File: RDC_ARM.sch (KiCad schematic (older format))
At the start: 38 parts, among them J1 RESOLVER ARM, Q1 BC807, Q2 BC807, U1 AD8397ARZ, X1 8.192MHz

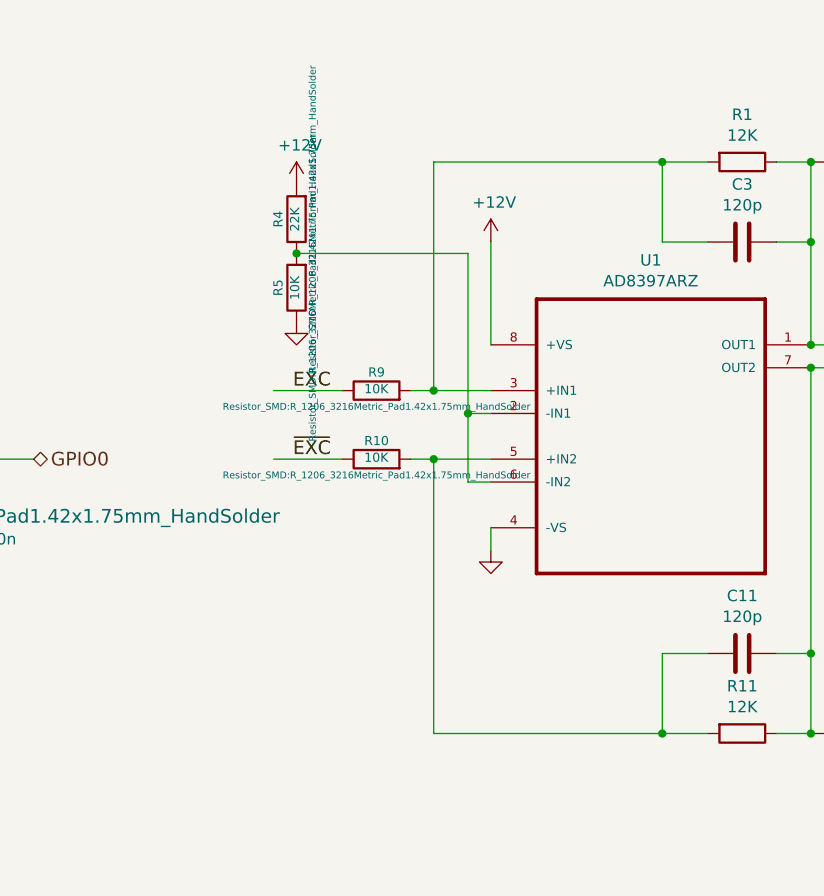
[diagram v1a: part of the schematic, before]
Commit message: Se arregló conexion erronea en los amplificadores operacionales
se agregó conexión 1-wire en GPIO8
se agregó botón y led que comparten GPIO7, la idea es leer el estado del
botón y al liberarlo cambiar el GPIO a output y encender el led indicando
alguna acción
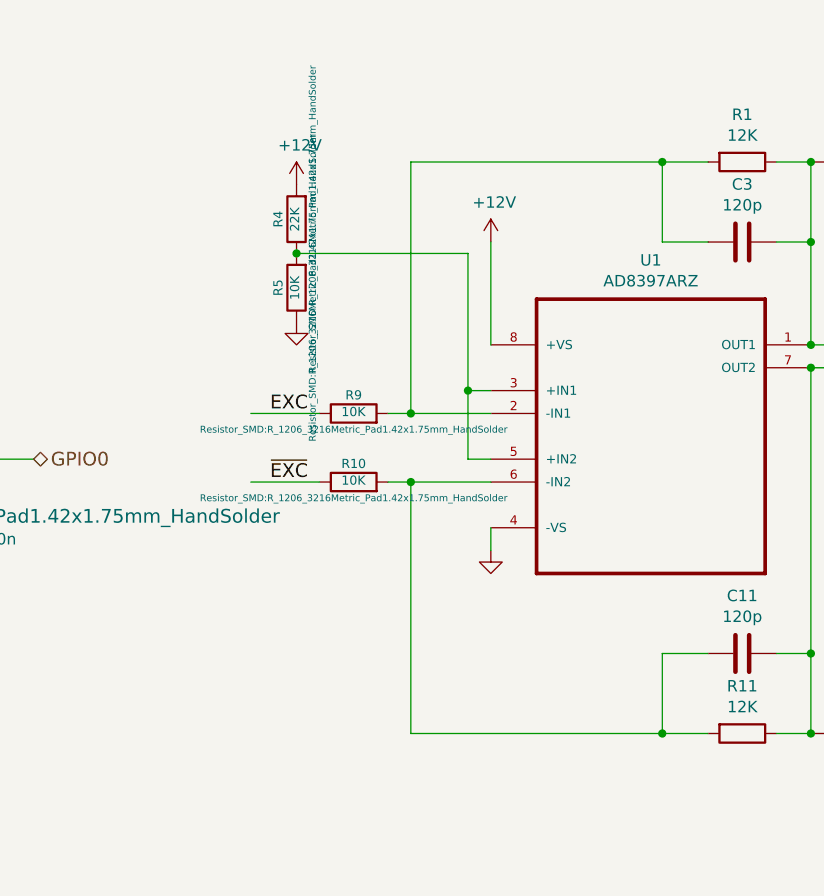
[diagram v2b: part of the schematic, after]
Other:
- moved on the sheet: R10, R9
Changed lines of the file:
@@
 Wire Wire Line
 	8550 4550 8550 4650
-Text Label 7850 4250 2    60   ~ 0
+Text Label 7750 4350 2    60   ~ 0
 ~EXC
-Wire Wire Line
-	8450 4350 8550 4350
 Wire Wire Line
 	7700 3350 8450 3350
@@
 	9950 5450 9800 5450
 Wire Wire Line
-	8300 4250 8550 4250
-Wire Wire Line
 	4750 2050 5100 2050
 Connection ~ 4750 2050
@@
 L Device:R R?
 U 1 1 5F08F1F2
-P 8050 4250
+P 7950 4350
 AR Path="/5F08F1F2" Ref="R?"  Part="1"
 AR Path="/5EF45E27/5F08F1F2" Ref="R10"  Part="1"
 AR Path="/5F077C82/5F08F1F2" Ref="R?"  Part="1"
-F 0 "R10" V 8130 4250 40  0000 C CNN
-F 1 "10K" V 8057 4251 40  0000 C CNN
-F 2 "Resistor_SMD:R_1206_3216Metric_Pad1.42x1.75mm_HandSolder" V 7980 4250 30  0000 C CNN
-F 3 "~" H 8050 4250 30  0000 C CNN
-	1    8050 4250
+F 0 "R10" V 8030 4350 40  0000 C CNN
+F 1 "10K" V 7957 4351 40  0000 C CNN
+F 2 "Resistor_SMD:R_1206_3216Metric_Pad1.42x1.75mm_HandSolder" V 7880 4350 30  0000 C CNN
+F 3 "~" H 7950 4350 30  0000 C CNN
+	1    7950 4350
 	0    -1   -1   0
 $EndComp
@@
 L Device:R R?
 U 1 1 5F08F1F3
-P 8050 3950
+P 7950 4050
 AR Path="/5F08F1F3" Ref="R?"  Part="1"
 AR Path="/5EF45E27/5F08F1F3" Ref="R9"  Part="1"
 AR Path="/5F077C82/5F08F1F3" Ref="R?"  Part="1"
-F 0 "R9" V 8130 3950 40  0000 C CNN
-F 1 "10K" V 8057 3951 40  0000 C CNN
-F 2 "Resistor_SMD:R_1206_3216Metric_Pad1.42x1.75mm_HandSolder" V 7980 3950 30  0000 C CNN
-F 3 "~" H 8050 3950 30  0000 C CNN
-	1    8050 3950
+F 0 "R9" V 8030 4050 40  0000 C CNN
+F 1 "10K" V 7957 4051 40  0000 C CNN
+F 2 "Resistor_SMD:R_1206_3216Metric_Pad1.42x1.75mm_HandSolder" V 7880 4050 30  0000 C CNN
+F 3 "~" H 7950 4050 30  0000 C CNN
+	1    7950 4050
 	0    -1   -1   0
 $EndComp
@@
 	8550 3300 8550 3750
 Wire Wire Line
-	8200 3950 8300 3950
-Connection ~ 8300 3950
-Wire Wire Line
-	8200 4250 8300 4250
-Connection ~ 8300 4250
-Wire Wire Line
-	7600 3950 7900 3950
-Wire Wire Line
-	7900 4250 7600 4250
+	8100 4050 8200 4050
+Connection ~ 8200 4050
+Wire Wire Line
+	8100 4350 8200 4350
+Connection ~ 8200 4350
+Wire Wire Line
+	7500 4050 7800 4050
+Wire Wire Line
+	7800 4350 7500 4350
 Text Label 10600 4350 2    60   ~ 0
 COS
@@
 Wire Wire Line
 	9300 2950 9500 2950
-Wire Wire Line
-	8300 2950 9300 2950
 $Comp
 L power:GND #PWR?
@@
 Wire Wire Line
 	9300 5450 9500 5450
-Wire Wire Line
-	8300 5450 9300 5450
 Connection ~ 9300 5450
 Wire Wire Line
-	8300 4250 8300 5450
+	8200 4350 8200 5450
 Wire Wire Line
 	9950 3850 9950 5100
@@
 Text Notes 4450 2700 0    60   ~ 0
 A0/A1\n 0  0 Normal mode—position output\n 0  1 Normal mode—velocity output\n 1  0 Reserved\n 1  1 Configuration mode
-Connection ~ 8450 4050
-Wire Wire Line
-	8450 4050 8450 4350
-Wire Wire Line
-	8450 4050 8550 4050
-Wire Wire Line
-	8300 2950 8300 3950
-Wire Wire Line
-	8300 3950 8550 3950
-Wire Wire Line
-	8450 3350 8450 4050
-Text Label 7850 3950 2    60   ~ 0
+Text Label 7750 4050 2    60   ~ 0
 EXC
 Wire Wire Line
@@
 	1    0    0    -1
 $EndComp
+Wire Wire Line
+	8200 4350 8550 4350
+Wire Wire Line
+	8200 2950 9300 2950
+Wire Wire Line
+	8200 2950 8200 4050
+Wire Wire Line
+	8200 4050 8550 4050
+Wire Wire Line
+	8550 4250 8450 4250
+Wire Wire Line
+	8450 4250 8450 3950
+Wire Wire Line
+	8550 3950 8450 3950
+Connection ~ 8450 3950
+Wire Wire Line
+	8450 3950 8450 3350
+Wire Wire Line
+	8200 5450 9300 5450
 $EndSCHEMATC
